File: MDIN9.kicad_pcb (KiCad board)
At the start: 2 copper layers, 110 x 50 mm, 40 parts, among them CN1 9, CN2 9, CN3 35RAPC4BH3, CN5 B6B-XH-A(LF)(SN), CN6 353180620, J1A JAMMA PINS 3.96MM PITCH 2.2MM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, J1B JAMMA PINS 3.96MM PITCH 2.2MM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, SW1 MJTP1230, SW2 MJTP1230, SW3 A6H-4101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

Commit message: Full route
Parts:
- removed the ? at (3.00, -7.00)
- removed the ? at (107.0, -7.00)
- added ?: , AutoGenerated:MountingHole_3.00mm, F.Cu at (4.00, -19.0)
- added ?: , AutoGenerated:MountingHole_3.00mm, F.Cu at (106.0, -19.0)
- SW3: value A6H-4101 -> DIPSwitch-4; footprint easyeda:A6H-4101 -> MinigunParts:DIPSwitch-4
- moved CN3 29.6 mm to (6.75, -10.8)
- moved H3 12.3 mm to (11.5, -18.5)
- moved CN1 11.9 mm to (78.0, -12.2)
- moved CN2 11.9 mm to (36.0, -12.2)
- moved SW3 9.83 mm to (28.0, 21.2), turned to 270 degrees
- moved H1 7.00 mm to (67.3, -2.50)
- moved VOLTMETER 7.00 mm to (76.0, 2.00)
- moved SW1 6.88 mm to (101.8, -12.0)
- moved SW2 6.17 mm to (101.8, -2.25)
- moved SW4 2.14 mm to (49.2, 25.8), turned to 180 degrees
- moved CN5 0.30 mm to (9.00, 30.0)
- turned R7 to 270 degrees
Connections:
- SW3 pad 2: P1_B5_J -> P1_B4
- SW3 pad 3: P1_B4 -> P2_B5
- SW3 pad 4: P1_B4_J -> P2_B4
- SW3 pad 5: P2_B5 -> P2_B4_J
- SW3 pad 7: P2_B4 -> P1_B4_J
- SW3 pad 8: P2_B4_J -> P1_B5_J
- U1 pad 11: VIDEO_RED_3 -> VIDEO_GREEN_3
- U1 pad 12: VIDEO_GREEN_3 -> VIDEO_BLUE_3
- U1 pad 13: VIDEO_BLUE_3 -> VIDEO_RED_3
- U1 pad 2: VIDEO_BLUE_2 -> VIDEO_RED_2
- U1 pad 3: VIDEO_GREEN_2 -> VIDEO_BLUE_2
- U1 pad 4: VIDEO_RED_2 -> VIDEO_GREEN_2
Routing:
- net GND: track 293.1 -> 87.6 mm, vias 2 -> 9
- net P2_START: track 42.4 -> 111.8 mm, vias 1 -> 3
- net +5V: track 246.1 -> 177.5 mm, vias 0 -> 2
- net P1_LEFT: track 70.7 -> 122.4 mm, vias 3 -> 5
- net P2_LEFT: track 44.0 -> 81.2 mm, vias 1 -> 3
- net P2_RIGHT: track 37.0 -> 72.6 mm, vias 2 -> 4
- net P1_COIN: track 51.1 -> 82.9 mm, vias 2 -> 3
- net P1_UP: track 59.9 -> 89.0 mm
- net P1_B1: track 86.6 -> 114.9 mm
- net P1_B4_J: track 16.9 -> 44.9 mm, vias 0 -> 3
- net P2_UP: track 54.4 -> 80.4 mm, vias 1 -> 4
- net P2_B1: track 50.4 -> 76.3 mm, vias 2 -> 1
- net P1_B4: track 86.1 -> 105.7 mm
- net P2_B2: track 88.0 -> 68.8 mm, vias 0 -> 2
- net SP-_3: track 119.9 -> 139.0 mm, vias 0 -> 2
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- added copper zone on F.Cu, net +5V
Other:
- board size 110 x 50 mm -> 110 x 62 mm
- board text added: "ADVANCED EDITION + HD15 RGBS"
- board text added: "CS"
- board text removed: "ADVANCED EDITION"

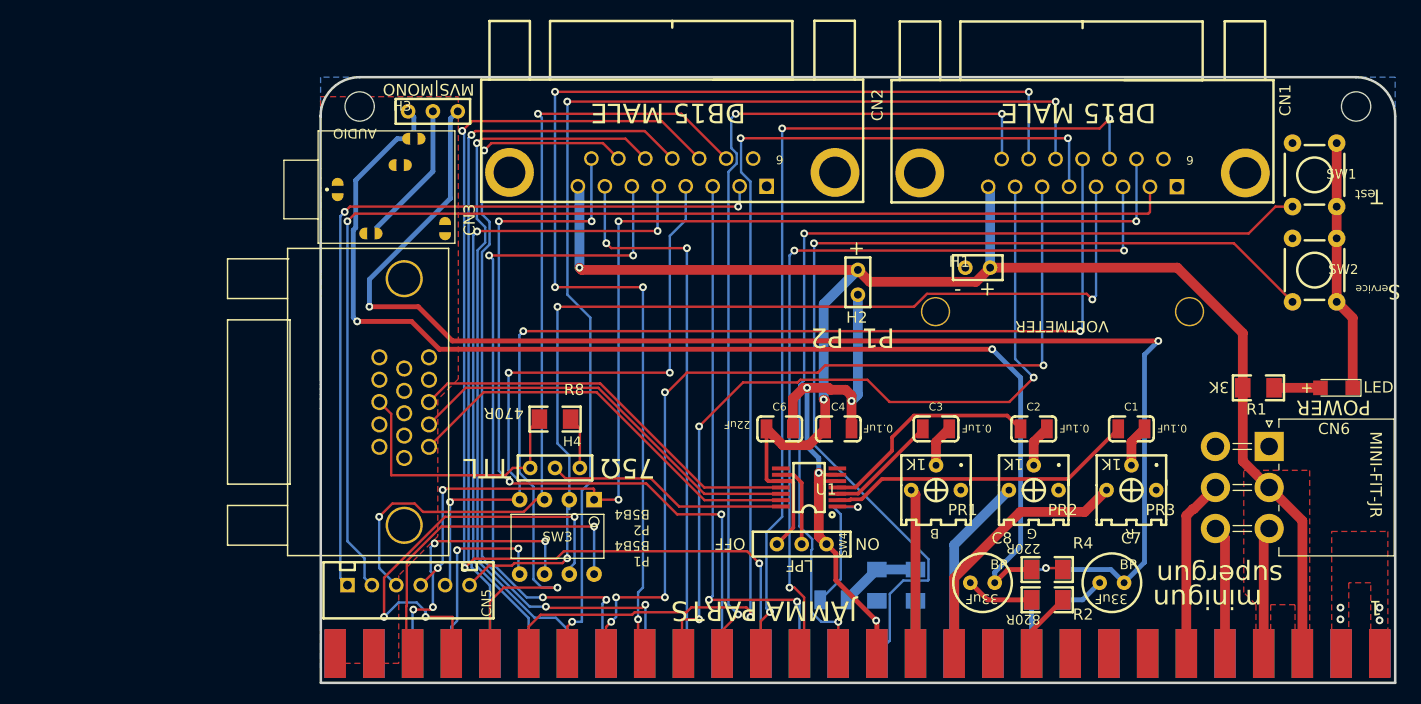
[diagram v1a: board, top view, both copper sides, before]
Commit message: Decoupling caps for R, G, B
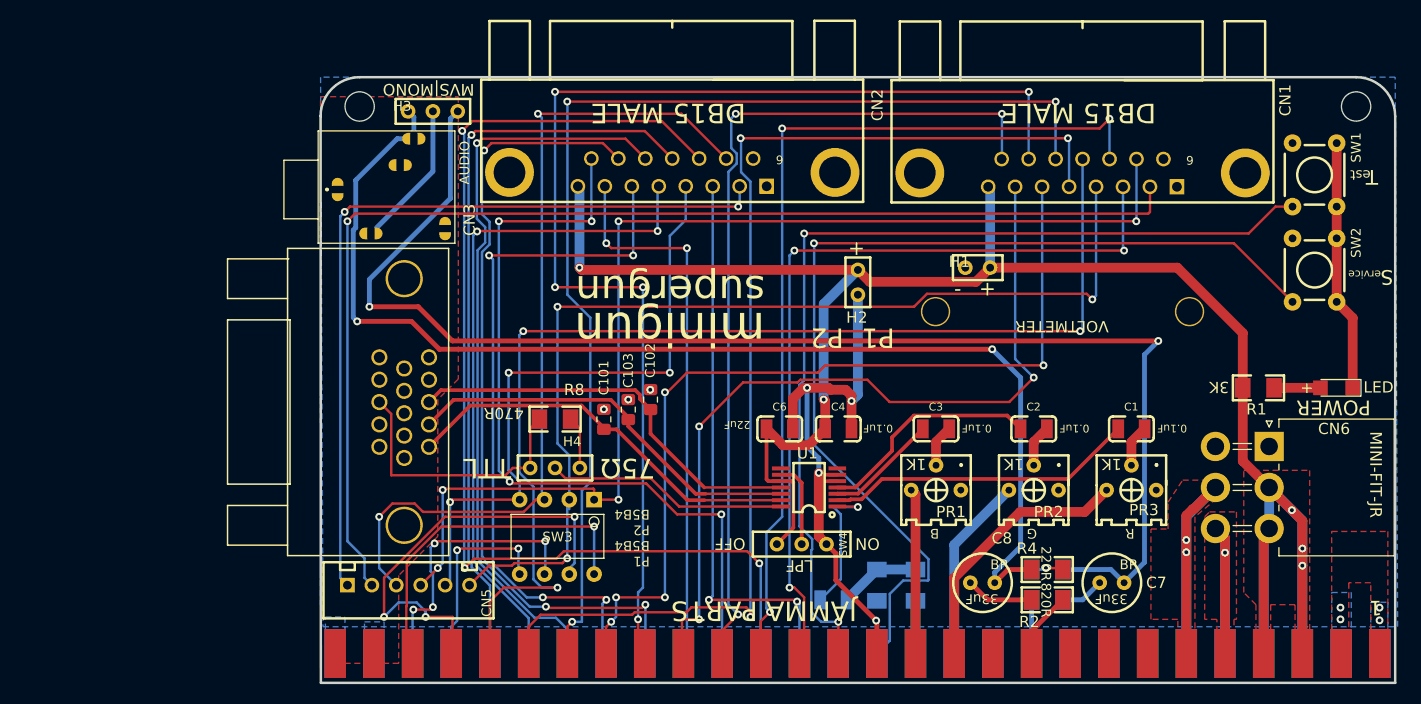
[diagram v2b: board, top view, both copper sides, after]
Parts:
- added C101: C_0805_2012Metric_Pad1.15x1.40mm_HandSolder, Capacitor_SMD:C_0805_2012Metric_Pad1.15x1.40mm_HandSolder, F.Cu at (29.0, 13.0)
- added C102: C_0805_2012Metric_Pad1.15x1.40mm_HandSolder, Capacitor_SMD:C_0805_2012Metric_Pad1.15x1.40mm_HandSolder, F.Cu at (33.8, 11.0)
- added C103: C_0805_2012Metric_Pad1.15x1.40mm_HandSolder, Capacitor_SMD:C_0805_2012Metric_Pad1.15x1.40mm_HandSolder, F.Cu at (31.5, 12.0)
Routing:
- net +5V: track 177.5 -> 213.2 mm, vias 2 -> 5
- net +12V: track 18.3 -> 36.5 mm, vias 0 -> 2
- net -5V: track 13.2 -> 26.4 mm, vias 0 -> 1
- net VIDEO_GREEN_3: track 41.2 -> 42.3 mm
- net VIDEO_RED_3: track 42.9 -> 41.9 mm
- net GND: vias 9 -> 12
- added copper zone on F.Cu, net +12V
- added copper zone on F.Cu, net -5V
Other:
- board text added: "REV_2.5+HD15_0.2"
- board text removed: "REV_2.5+HD15"

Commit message: Coupling caps, series resistors for rgb
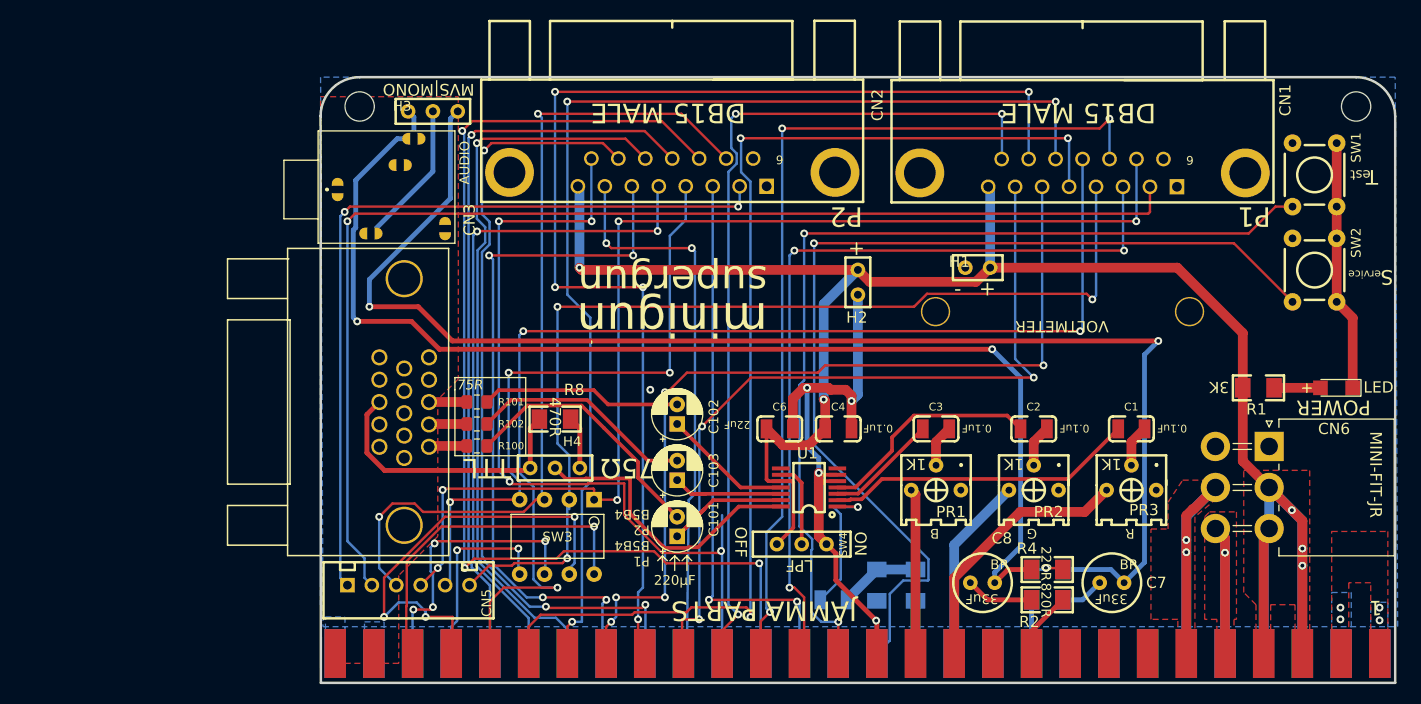
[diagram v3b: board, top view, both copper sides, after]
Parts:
- added R100: R_0805_2012Metric_Pad1.15x1.40mm_HandSolder, Resistor_SMD:R_0805_2012Metric_Pad1.15x1.40mm_HandSolder, F.Cu at (16.0, 15.8)
- added R101: R_0805_2012Metric_Pad1.15x1.40mm_HandSolder, Resistor_SMD:R_0805_2012Metric_Pad1.15x1.40mm_HandSolder, F.Cu at (16.0, 11.2)
- added R102: R_0805_2012Metric_Pad1.15x1.40mm_HandSolder, Resistor_SMD:R_0805_2012Metric_Pad1.15x1.40mm_HandSolder, F.Cu at (16.0, 13.5)
- C101, C102, C103: value C_0805_2012Metric_Pad1.15x1.40mm_HandSolder -> CP_Radial_D5.0mm_P2.00mm; footprint Capacitor_SMD:C_0805_2012Metric_Pad1.15x1.40mm_HandSolder -> Capacitor_THT:CP_Radial_D5.0mm_P2.00mm
- moved C101 14.1 mm to (36.5, 25.0), turned to 90 degrees
- moved C103 8.79 mm to (36.5, 19.2), turned to 90 degrees
- moved C102 3.70 mm to (36.5, 13.5), turned to 90 degrees
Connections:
- C101 pad 1: GND -> VIDEO_RED_3
- C101 pad 2: VIDEO_RED_3 -> VIDEO_RED_4
- C102 pad 1: GND -> VIDEO_GREEN_3
- C102 pad 2: VIDEO_GREEN_3 -> VIDEO_GREEN_4
- C103 pad 1: GND -> VIDEO_BLUE_3
- C103 pad 2: VIDEO_BLUE_3 -> VIDEO_BLUE_4
- REF** pad 1: VIDEO_RED_3 -> VIDEO_RED_5
- REF** pad 2: VIDEO_BLUE_3 -> VIDEO_BLUE_5
- REF** pad 3: VIDEO_GREEN_3 -> VIDEO_GREEN_5
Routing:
- net VIDEO_GREEN_3: track 42.3 -> 13.7 mm
- net VIDEO_RED_4: track 0.00 -> 26.8 mm
- net VIDEO_RED_3: track 41.9 -> 16.1 mm
- net VIDEO_BLUE_4: track 0.00 -> 23.5 mm
- net VIDEO_BLUE_3: track 41.7 -> 20.5 mm
- net VIDEO_GREEN_4: track 0.00 -> 20.6 mm
- net VIDEO_SYNC_3: track 24.7 -> 35.4 mm
- net VIDEO_RED_5: track 0.00 -> 3.91 mm
- net VIDEO_BLUE_5: track 0.00 -> 3.89 mm
- net VIDEO_GREEN_5: track 0.00 -> 3.88 mm
- net P2_UP: track 80.4 -> 83.9 mm
- net P1_DOWN: track 83.6 -> 81.5 mm
- net P2_DOWN: track 56.0 -> 56.9 mm
- net VIDEO_SYNC_5: track 27.9 -> 28.7 mm
- net GND: vias 12 -> 10
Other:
- board text added: "220µF"
- board text added: "75R"

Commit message: Send v0.2 to fab
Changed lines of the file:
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@@
       (drillshape 0)
       (scaleselection 1)
-      (outputdirectory "hd15-minigun-v0.1"))
+      (outputdirectory "hd15-minigun-v0.2"))
   )
   (net 0 "")
@@
       (effects (font (size 1.15 1.15) (thickness 0.15)) (justify left))
     )
-    (fp_text value BP (at 0.786 -1.85 180) (layer F.SilkS)
+    (fp_text value BP (at -1.1 -1.85 180) (layer F.SilkS)
       (effects (font (size 1 1) (thickness 0.15)) (justify left))
     )
@@
       (effects (font (size 1.15 1.15) (thickness 0.15)) (justify left))
     )
-    (fp_text value BP (at 0.786 -1.85 180) (layer F.SilkS)
+    (fp_text value BP (at -1.16 -1.85 180) (layer F.SilkS)
       (effects (font (size 1 1) (thickness 0.15)) (justify left))
     )
@@
   (module easyeda:TACTILE-PTH (layer F.Cu)
     (at 101.75 -12 270)
-    (fp_text reference SW1 (at -1.25 -4.25 90) (layer F.SilkS)
+    (fp_text reference SW1 (at 1.5 0 90) (layer F.SilkS)
       (effects (font (size 1 1) (thickness 0.12)) (justify left))
     )
@@
   (module easyeda:TACTILE-PTH (layer F.Cu)
     (at 101.75 -2.25 270)
-    (fp_text reference SW2 (at -1.25 -4.25 270) (layer F.SilkS)
+    (fp_text reference SW2 (at 1.55 0 270) (layer F.SilkS)
       (effects (font (size 1 1) (thickness 0.12)) (justify left))
     )
@@
     (polygon
       (pts
-        (xy 101.25 37.5) (xy 99.75 37.5) (xy 99.75 32) (xy 97.25 32) (xy 97.25 37.5)
-        (xy 95.75 37.5) (xy 95.75 32) (xy 94.5 30.75) (xy 94.5 18.25) (xy 101.25 18.25)
+        (xy 101.4 38.525) (xy 99.75 37.5) (xy 99.75 32) (xy 97.25 32) (xy 97.25 37.5)
+        (xy 95.75 37.5) (xy 95.75 32) (xy 94.5 30.75) (xy 94.5 18.25) (xy 101.4 19.275)
       )
     )
@@
       )
     )
+  )
+  (zone (net 2) (net_name +5V) (layer F.Cu) (hatch edge 0.508)
+    (connect_pads (clearance 0.254))
+    (min_thickness 0.254)
+    (fill yes (arc_segments 32) (thermal_gap 0.508) (thermal_bridge_width 0.508))
+    (polygon
+      (pts
+        (xy 106.2 23.8) (xy 102.7 23.8) (xy 102.7 32) (xy 99.3 32) (xy 99.3 15.3)
+        (xy 106.2 15.3)
+      )
+    )
